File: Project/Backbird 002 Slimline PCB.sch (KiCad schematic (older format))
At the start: 8 parts

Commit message: Upgraded project to KiCad 5 RC2 nightly build (kicad-20180606-033155.9552e02-c4osx)
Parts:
- D1: symbol LED -> Backbird-002-Slimline-PCB-rescue:LED
- Molex_4pin1: symbol Conn_01x04 -> Backbird-002-Slimline-PCB-rescue:Conn_01x04
- R1, R2: symbol R -> Backbird-002-Slimline-PCB-rescue:R
- Sata1, Sata2, SataSlimline1: symbol Conn_01x06 -> Backbird-002-Slimline-PCB-rescue:Conn_01x06
- SataSlimline_Power1: symbol Conn_01x07 -> Backbird-002-Slimline-PCB-rescue:Conn_01x07
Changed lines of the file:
@@
-EESchema Schematic File Version 2
-LIBS:power
-LIBS:device
-LIBS:transistors
-LIBS:conn
-LIBS:linear
-LIBS:regul
-LIBS:74xx
-LIBS:cmos4000
-LIBS:adc-dac
-LIBS:memory
-LIBS:xilinx
-LIBS:microcontrollers
-LIBS:dsp
-LIBS:microchip
-LIBS:analog_switches
-LIBS:motorola
-LIBS:texas
-LIBS:intel
-LIBS:audio
-LIBS:interface
-LIBS:digital-audio
-LIBS:philips
-LIBS:display
-LIBS:cypress
-LIBS:siliconi
-LIBS:opto
-LIBS:atmel
-LIBS:contrib
-LIBS:valves
+EESchema Schematic File Version 4
 LIBS:Backbird 002 Slimline PCB-cache
-EELAYER 25 0
+EELAYER 26 0
 EELAYER END
 $Descr A4 11693 8268
@@
 $EndDescr
 $Comp
-L R R1
+L Backbird-002-Slimline-PCB-rescue:R R1
 U 1 1 5B10C22E
 P 2600 1850
@@
 $EndComp
 $Comp
-L R R2
+L Backbird-002-Slimline-PCB-rescue:R R2
 U 1 1 5B10C260
 P 2600 2350
@@
 $EndComp
 $Comp
-L LED D1
+L Backbird-002-Slimline-PCB-rescue:LED D1
 U 1 1 5B10C28E
 P 2900 2100
@@
 $EndComp
 $Comp
-L Conn_01x04 Molex_4pin1
+L Backbird-002-Slimline-PCB-rescue:Conn_01x04 Molex_4pin1
 U 1 1 5B10C5B0
 P 2950 4450
@@
 +12V\nGND\nGND\n+5V
 $Comp
-L Conn_01x06 Sata1
+L Backbird-002-Slimline-PCB-rescue:Conn_01x06 Sata1
 U 1 1 5B10CD9C
 P 5100 4300
@@
 $EndComp
 $Comp
-L Conn_01x06 SataSlimline1
+L Backbird-002-Slimline-PCB-rescue:Conn_01x06 SataSlimline1
 U 1 1 5B10CE60
 P 5800 1650
@@
 $EndComp
 $Comp
-L Conn_01x07 SataSlimline_Power1
+L Backbird-002-Slimline-PCB-rescue:Conn_01x07 SataSlimline_Power1
 U 1 1 5B10CE99
 P 2950 3500
@@
 Coding\nDevice Presence\n+5V\n+5V\nDiagnostics\nGND\nGND
 $Comp
-L Conn_01x06 Sata2
+L Backbird-002-Slimline-PCB-rescue:Conn_01x06 Sata2
 U 1 1 5B10D3FA
 P 5100 5100
@@
 $EndComp
 Wire Wire Line
-	2600 2000 2600 2200
+	2600 2000 2600 2100
 Wire Wire Line
 	2750 2100 2600 2100
 Connection ~ 2600 2100
 Wire Wire Line
-	2600 2500 2600 4650
+	2600 2500 2600 3500
 Wire Wire Line
 	2600 4650 2750 4650
@@
 Connection ~ 3200 2100
 Wire Wire Line
-	3200 1700 3200 4150
+	3200 1700 3200 2100
 Wire Wire Line
 	3200 4150 2700 4150
 Wire Wire Line
-	2700 3700 2700 4550
+	2700 3700 2700 3800
 Wire Wire Line
 	2700 4550 2750 4550
@@
 Connection ~ 2700 3800
 Wire Wire Line
-	2600 3500 2750 3500
+	2600 3500 2700 3500
 Connection ~ 2600 3500
 Wire Wire Line
@@
 Connection ~ 2700 3500
 Wire Wire Line
-	4900 4100 5500 4100
-Wire Wire Line
-	4850 4200 5450 4200
-Wire Wire Line
-	4800 4300 5400 4300
-Wire Wire Line
-	4750 4400 5350 4400
+	4900 4100 5300 4100
+Wire Wire Line
+	4850 4200 5300 4200
+Wire Wire Line
+	4800 4300 5300 4300
+Wire Wire Line
+	4750 4400 5300 4400
 Wire Wire Line
 	4950 1950 5600 1950
@@
 	5550 5400 5550 4000
 Wire Wire Line
-	5550 4000 4950 4000
+	5550 4000 5300 4000
 Wire Wire Line
 	4950 4000 4950 1950
@@
 Connection ~ 2700 4450
 NoConn ~ 2750 4350
+Wire Wire Line
+	2600 2100 2600 2200
+Wire Wire Line
+	3200 2100 3200 4150
+Wire Wire Line
+	2700 4150 2700 4450
+Wire Wire Line
+	2700 3800 2700 4150
+Wire Wire Line
+	2600 3500 2600 4650
+Wire Wire Line
+	2700 3500 2750 3500
+Wire Wire Line
+	5300 4400 5350 4400
+Wire Wire Line
+	5300 4300 5400 4300
+Wire Wire Line
+	5300 4200 5450 4200
+Wire Wire Line
+	5300 4100 5500 4100
+Wire Wire Line
+	5300 4000 4950 4000
+Wire Wire Line
+	2700 4450 2700 4550
 $EndSCHEMATC

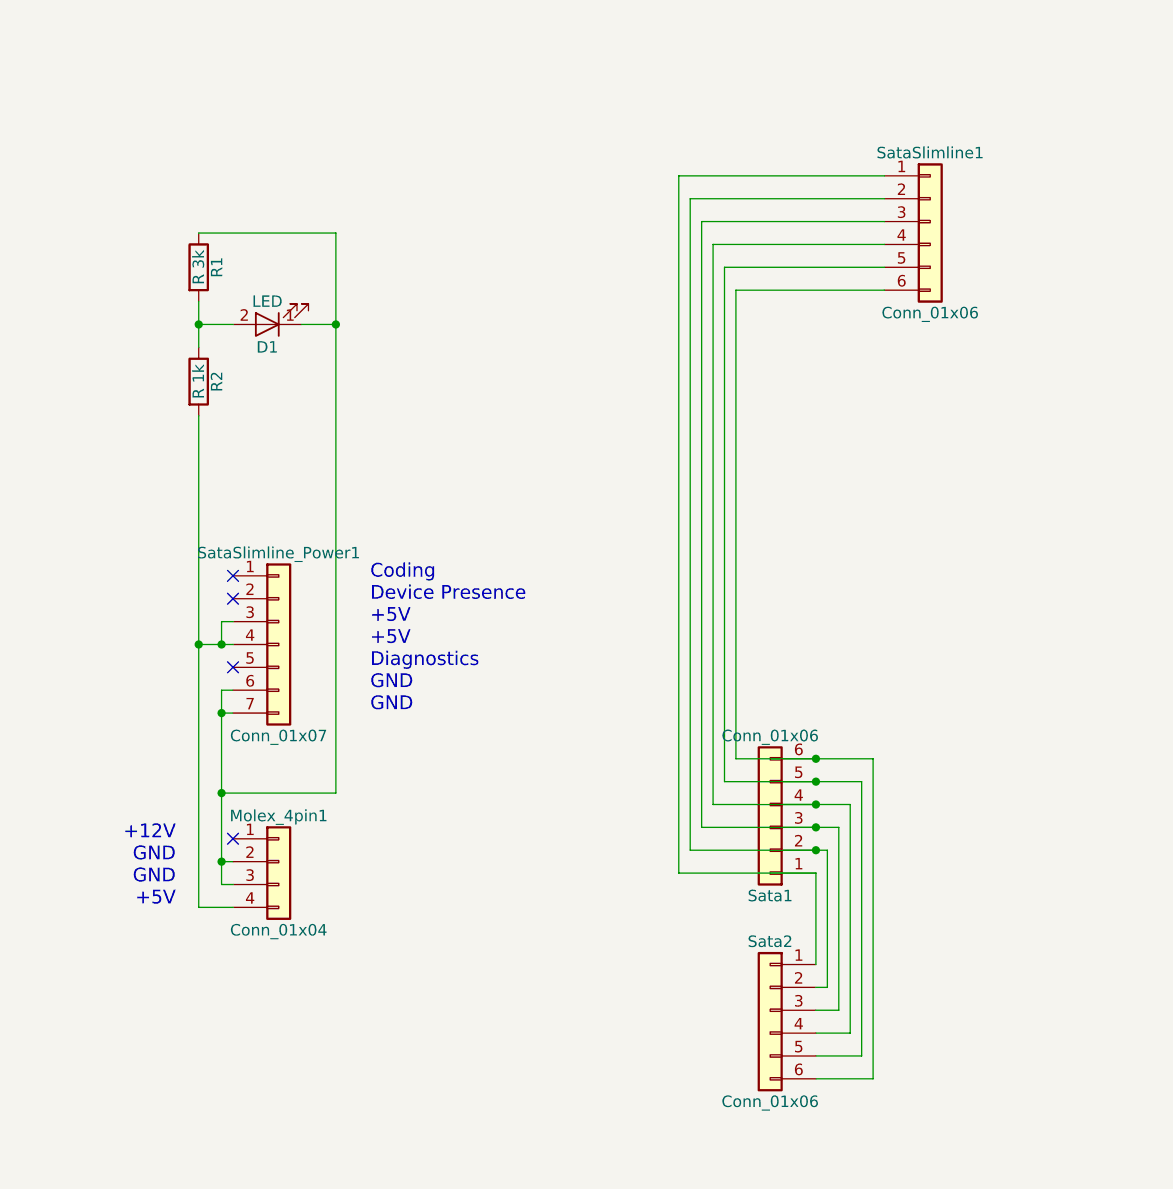
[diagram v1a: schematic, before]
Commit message: Fixed pinout of Sata data ports to be 7-pin instead of 6
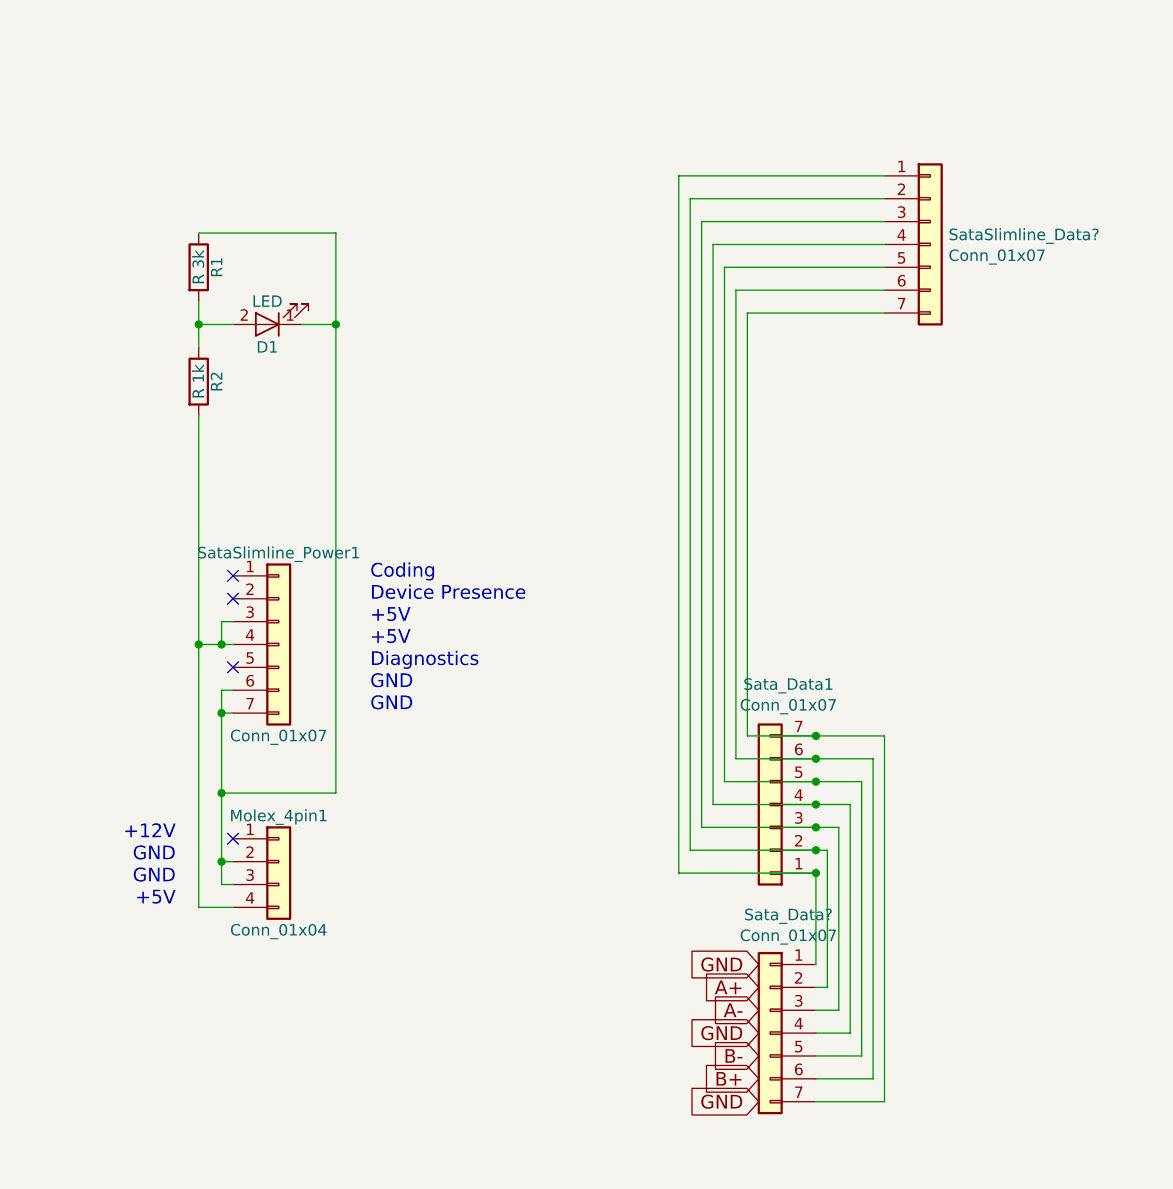
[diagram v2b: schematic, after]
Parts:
- removed Sata1, Sata2, SataSlimline1: Conn_01x06, Connectors:SATA-7_THT_VERT_2, symbol Backbird-002-Slimline-PCB-rescue:Conn_01x06
- added SataSlimline_Data?, Sata_Data1, Sata_Data?: Conn_01x07, symbol Backbird-002-Slimline-PCB-rescue:Conn_01x07
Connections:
- new net: SataSlimline_Data?.1 (Pin_1), Sata_Data1.1 (Pin_1), Sata_Data?.1 (Pin_1)
- new net: SataSlimline_Data?.2 (Pin_2), Sata_Data1.2 (Pin_2), Sata_Data?.2 (Pin_2)
- new net: SataSlimline_Data?.3 (Pin_3), Sata_Data1.3 (Pin_3), Sata_Data?.3 (Pin_3)
- new net: SataSlimline_Data?.4 (Pin_4), Sata_Data1.4 (Pin_4), Sata_Data?.4 (Pin_4)
- new net: SataSlimline_Data?.5 (Pin_5), Sata_Data1.5 (Pin_5), Sata_Data?.5 (Pin_5)
- new net: SataSlimline_Data?.6 (Pin_6), Sata_Data1.6 (Pin_6), Sata_Data?.6 (Pin_6)
- new net: SataSlimline_Data?.7 (Pin_7), Sata_Data1.7 (Pin_7), Sata_Data?.7 (Pin_7)
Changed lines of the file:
@@
 +12V\nGND\nGND\n+5V
-$Comp
-L Backbird-002-Slimline-PCB-rescue:Conn_01x06 Sata1
-U 1 1 5B10CD9C
-P 5100 4300
-F 0 "Sata1" H 5100 4600 50  0000 C CNN
-F 1 "Conn_01x06" H 5100 3900 50  0000 C CNN
-F 2 "Connectors:SATA-7_THT_VERT_2" H 5100 4300 50  0001 C CNN
-F 3 "" H 5100 4300 50  0001 C CNN
-	1    5100 4300
-	-1   0    0    1
-$EndComp
-$Comp
-L Backbird-002-Slimline-PCB-rescue:Conn_01x06 SataSlimline1
-U 1 1 5B10CE60
-P 5800 1650
-F 0 "SataSlimline1" H 5800 1950 50  0000 C CNN
-F 1 "Conn_01x06" H 5800 1250 50  0000 C CNN
-F 2 "Connectors:SATA-7_THT_VERT_2" H 5800 1650 50  0001 C CNN
-F 3 "" H 5800 1650 50  0001 C CNN
-	1    5800 1650
-	1    0    0    -1
-$EndComp
 $Comp
 L Backbird-002-Slimline-PCB-rescue:Conn_01x07 SataSlimline_Power1
@@
 Text Notes 3350 3800 0    60   ~ 0
 Coding\nDevice Presence\n+5V\n+5V\nDiagnostics\nGND\nGND
-$Comp
-L Backbird-002-Slimline-PCB-rescue:Conn_01x06 Sata2
-U 1 1 5B10D3FA
-P 5100 5100
-F 0 "Sata2" H 5100 5400 50  0000 C CNN
-F 1 "Conn_01x06" H 5100 4700 50  0000 C CNN
-F 2 "Connectors:SATA-7_THT_VERT_2" H 5100 5100 50  0001 C CNN
-F 3 "" H 5100 5100 50  0001 C CNN
-	1    5100 5100
-	-1   0    0    -1
-$EndComp
 Wire Wire Line
 	2600 2000 2600 2100
@@
 Wire Wire Line
 	5400 5100 5400 4300
-Connection ~ 5300 4300
 Wire Wire Line
 	5300 5200 5450 5200
 Wire Wire Line
 	5450 5200 5450 4200
-Connection ~ 5300 4200
 Wire Wire Line
 	5300 5300 5500 5300
 Wire Wire Line
 	5500 5300 5500 4100
-Connection ~ 5300 4100
 Wire Wire Line
 	5300 5400 5550 5400
@@
 Wire Wire Line
 	4950 4000 4950 1950
-Connection ~ 5300 4000
 NoConn ~ 2750 3600
 NoConn ~ 2750 3300
@@
 Wire Wire Line
 	2700 4450 2700 4550
+$Comp
+L Backbird-002-Slimline-PCB-rescue:Conn_01x07 Sata_Data1
+U 1 1 5B19C63F
+P 5100 4200
+F 0 "Sata_Data1" H 5020 3675 50  0000 C CNN
+F 1 "Conn_01x07" H 5020 3766 50  0000 C CNN
+F 2 "" H 5100 4200 50  0001 C CNN
+F 3 "" H 5100 4200 50  0001 C CNN
+	1    5100 4200
+	-1   0    0    1
+$EndComp
+Connection ~ 5300 4500
+$Comp
+L Backbird-002-Slimline-PCB-rescue:Conn_01x07 Sata_Data?
+U 1 1 5B19E3C5
+P 5100 5200
+F 0 "Sata_Data?" H 5020 5717 50  0000 C CNN
+F 1 "Conn_01x07" H 5020 5626 50  0000 C CNN
+F 2 "" H 5100 5200 50  0001 C CNN
+F 3 "" H 5100 5200 50  0001 C CNN
+	1    5100 5200
+	-1   0    0    -1
+$EndComp
+Wire Wire Line
+	5300 5500 5600 5500
+Wire Wire Line
+	5600 5500 5600 3900
+Wire Wire Line
+	5600 3900 5300 3900
+$Comp
+L Backbird-002-Slimline-PCB-rescue:Conn_01x07 SataSlimline_Data?
+U 1 1 5B19F411
+P 5800 1750
+F 0 "SataSlimline_Data?" H 5880 1792 50  0000 L CNN
+F 1 "Conn_01x07" H 5880 1701 50  0000 L CNN
+F 2 "" H 5800 1750 50  0001 C CNN
+F 3 "" H 5800 1750 50  0001 C CNN
+	1    5800 1750
+	1    0    0    -1
+$EndComp
+Wire Wire Line
+	5600 2050 5000 2050
+Wire Wire Line
+	5000 2050 5000 3900
+Wire Wire Line
+	5000 3900 5300 3900
+Text GLabel 5050 4900 0    60   Input ~ 0
+GND
+Text GLabel 5050 5200 0    60   Input ~ 0
+GND
+Text GLabel 5050 5000 0    60   Input ~ 0
+A+
+Text GLabel 5050 5100 0    60   Input ~ 0
+A-
+Text GLabel 5050 5300 0    60   Input ~ 0
+B-
+Text GLabel 5050 5400 0    60   Input ~ 0
+B+
+Text GLabel 5050 5500 0    60   Input ~ 0
+GND
+Connection ~ 5300 3900
+Connection ~ 5300 4000
+Connection ~ 5300 4100
+Connection ~ 5300 4200
+Connection ~ 5300 4300
 $EndSCHEMATC

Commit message: Annotated schematic
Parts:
- gave numbers to parts that had none: 2
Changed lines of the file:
@@
 Connection ~ 5300 4500
 $Comp
-L Backbird-002-Slimline-PCB-rescue:Conn_01x07 Sata_Data?
+L Backbird-002-Slimline-PCB-rescue:Conn_01x07 Sata_Data2
 U 1 1 5B19E3C5
 P 5100 5200
-F 0 "Sata_Data?" H 5020 5717 50  0000 C CNN
+F 0 "Sata_Data2" H 5020 5717 50  0000 C CNN
 F 1 "Conn_01x07" H 5020 5626 50  0000 C CNN
 F 2 "" H 5100 5200 50  0001 C CNN
@@
 	5600 3900 5300 3900
 $Comp
-L Backbird-002-Slimline-PCB-rescue:Conn_01x07 SataSlimline_Data?
+L Backbird-002-Slimline-PCB-rescue:Conn_01x07 SataSlimline_Data1
 U 1 1 5B19F411
 P 5800 1750
-F 0 "SataSlimline_Data?" H 5880 1792 50  0000 L CNN
+F 0 "SataSlimline_Data1" H 5880 1792 50  0000 L CNN
 F 1 "Conn_01x07" H 5880 1701 50  0000 L CNN
 F 2 "" H 5800 1750 50  0001 C CNN

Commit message: Added holes for blocking off the LED. Also added an additional connector for power
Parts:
- added Hole1, Hole2: Conn_01x01, symbol Connector:Conn_01x01
- added Power_4pin1: Conn_01x04, Connectors_Molex:Molex_Pico-EZmate_04x1.20mm_Angled, symbol Backbird-002-Slimline-PCB-rescue:Conn_01x04
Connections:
- wire segments 63 -> 69
- no-connect marks 4 -> 3
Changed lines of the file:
@@
 	-1   0    0    1
-$EndComp
-$Comp
-L Backbird-002-Slimline-PCB-rescue:Conn_01x04 Molex_4pin1
-U 1 1 5B10C5B0
-P 2950 4450
-F 0 "Molex_4pin1" H 2950 4650 50  0000 C CNN
-F 1 "Conn_01x04" H 2950 4150 50  0000 C CNN
-F 2 "Connectors_Molex:Molex_Pico-EZmate_04x1.20mm_Angled" H 2950 4450 50  0001 C CNN
-F 3 "" H 2950 4450 50  0001 C CNN
-	1    2950 4450
-	1    0    0    -1
 $EndComp
 Text Notes 2500 4650 2    60   ~ 0
@@
 Connection ~ 2600 2100
 Wire Wire Line
-	2600 2500 2600 3500
-Wire Wire Line
-	2600 4650 2750 4650
+	2600 2500 2600 2800
 Wire Wire Line
 	3050 2100 3200 2100
@@
 	2700 3700 2700 3800
 Wire Wire Line
-	2700 4550 2750 4550
-Wire Wire Line
 	2700 3800 2750 3800
-Connection ~ 2700 4150
 Wire Wire Line
 	2700 3700 2750 3700
@@
 NoConn ~ 2750 3200
 Wire Wire Line
-	2750 4450 2700 4450
-Connection ~ 2700 4450
-NoConn ~ 2750 4350
-Wire Wire Line
 	2600 2100 2600 2200
 Wire Wire Line
-	3200 2100 3200 4150
-Wire Wire Line
-	2700 4150 2700 4450
+	3200 2100 3200 2800
 Wire Wire Line
 	2700 3800 2700 4150
@@
 Connection ~ 5300 4200
 Connection ~ 5300 4300
+$Comp
+L Backbird-002-Slimline-PCB-rescue:Conn_01x04 Power_4pin1
+U 1 1 5B1AF5DD
+P 3650 4450
+F 0 "Power_4pin1" H 3650 4650 50  0000 C CNN
+F 1 "Conn_01x04" H 3650 4150 50  0000 C CNN
+F 2 "Connectors_Molex:Molex_Pico-EZmate_04x1.20mm_Angled" H 3650 4450 50  0001 C CNN
+F 3 "" H 3650 4450 50  0001 C CNN
+	1    3650 4450
+	1    0    0    -1
+$EndComp
+Connection ~ 2700 4450
+Connection ~ 2700 4150
+Wire Wire Line
+	2700 4150 2700 4450
+Wire Wire Line
+	3450 4650 2750 4650
+Wire Wire Line
+	2600 4650 2750 4650
+Connection ~ 2750 4650
+Wire Wire Line
+	2750 4550 3450 4550
+Wire Wire Line
+	2700 4550 2750 4550
+Connection ~ 2750 4550
+Wire Wire Line
+	3450 4450 2750 4450
+Wire Wire Line
+	2750 4450 2700 4450
+Connection ~ 2750 4450
+$Comp
+L Backbird-002-Slimline-PCB-rescue:Conn_01x04 Molex_4pin1
+U 1 1 5B10C5B0
+P 2950 4450
+F 0 "Molex_4pin1" H 2950 4650 50  0000 C CNN
+F 1 "Conn_01x04" H 2950 4150 50  0000 C CNN
+F 2 "Connectors_Molex:Molex_Pico-EZmate_04x1.20mm_Angled" H 2950 4450 50  0001 C CNN
+F 3 "" H 2950 4450 50  0001 C CNN
+	1    2950 4450
+	1    0    0    -1
+$EndComp
+Wire Wire Line
+	2750 4350 3450 4350
+$Comp
+L Connector:Conn_01x01 Hole1
+U 1 1 5B1B7221
+P 2400 2800
+F 0 "Hole1" H 2750 2750 50  0000 R CNN
+F 1 "Conn_01x01" H 3000 2850 50  0000 R CNN
+F 2 "" H 2400 2800 50  0001 C CNN
+F 3 "~" H 2400 2800 50  0001 C CNN
+	1    2400 2800
+	-1   0    0    1
+$EndComp
+Connection ~ 2600 2800
+Wire Wire Line
+	2600 2800 2600 3500
+$Comp
+L Connector:Conn_01x01 Hole2
+U 1 1 5B1B7286
+P 3400 2800
+F 0 "Hole2" H 3480 2842 50  0000 L CNN
+F 1 "Conn_01x01" H 3480 2751 50  0000 L CNN
+F 2 "" H 3400 2800 50  0001 C CNN
+F 3 "~" H 3400 2800 50  0001 C CNN
+	1    3400 2800
+	1    0    0    -1
+$EndComp
+Connection ~ 3200 2800
+Wire Wire Line
+	3200 2800 3200 4150
 $EndSCHEMATC

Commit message: First pass at building the PCB using footprints. Fixed Sata Slimeline Recpt footprint by numbering the pins from 1-13 and adding mechanical pads. Made molex 8981 footprint cleaner by adding the notch.
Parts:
- removed SataSlimline_Data1, SataSlimline_Power1: Conn_01x07, symbol Backbird-002-Slimline-PCB-rescue:Conn_01x07
- added Sata_Slimline_Recpt1: Conn_01x13, ProjectFootprints:SATA_SLIMLINE_RECPT_1735539-2, symbol Connector:Conn_01x13
- added Screw_Hole_B, Screw_Hole_T?: Conn_01x01, symbol Connector:Conn_01x01
- +5V_Hole1: renamed from Hole1; footprint (none) -> Wire_Pads:SolderWirePad_single_1-2mmDrill
- D1: footprint (none) -> LEDs:LED_D1.8mm_W3.3mm_H2.4mm
- GND_Hole2: renamed from Hole2; footprint (none) -> Wire_Pads:SolderWirePad_single_1-2mmDrill
- Molex_4pin1: footprint Connectors_Molex:Molex_Pico-EZmate_04x1.20mm_Angled -> ProjectFootprints:MOLEX_8981_0015244745
- Power_4pin1: footprint Connectors_Molex:Molex_Pico-EZmate_04x1.20mm_Angled -> Wire_Pads:SolderWirePad_4xInline_1-2mmDrill
- R1, R2: footprint (none) -> Resistors_Universal:Resistor_SMD+THTuniversal_2512_RM10_HandSoldering
- Sata_Data1, Sata_Data2: footprint (none) -> ProjectFootprints:SATA_DATA_678007005_CustomPad
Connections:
- net labels added: +12V, +5V
- wire segments 69 -> 8
- no-connect marks 3 -> 4
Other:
- note removed: "+12V\nGND\nGND\n+5V"
- note removed: "Coding\nDevice Presence\n+5V\n+5V\nDiagnostics\nGND\nGND"
- moved on the sheet: D1, Molex_4pin1, Power_4pin1, R1, R2, Sata_Data1, Sata_Data2

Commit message: Updated PSB layout. (might remove extra power and Sata locations) Added custom footprints for screws and for a generic 8981 power pinout.
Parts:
- Power_4pin1: footprint Wire_Pads:SolderWirePad_4xInline_1-2mmDrill -> ProjectFootprints:MOLEX_8981_Generic
- Screw_Hole_B1: renamed from Screw_Hole_B; footprint (none) -> ProjectFootprints:Blackbird002_Slimline_PCB_Screw
- Screw_Hole_T1: renamed from Screw_Hole_T?; footprint (none) -> ProjectFootprints:Blackbird002_Slimline_PCB_Screw
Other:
- moved on the sheet: Power_4pin1
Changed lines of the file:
@@
 L Backbird-002-Slimline-PCB-rescue:Conn_01x04 Power_4pin1
 U 1 1 5B1AF5DD
-P 3900 5450
-F 0 "Power_4pin1" H 3900 5650 50  0000 C CNN
-F 1 "Conn_01x04" H 3900 5150 50  0000 C CNN
-F 2 "Wire_Pads:SolderWirePad_4xInline_1-2mmDrill" H 3900 5450 50  0001 C CNN
-F 3 "" H 3900 5450 50  0001 C CNN
-	1    3900 5450
+P 4550 5450
+F 0 "Power_4pin1" H 4550 5650 50  0000 C CNN
+F 1 "Conn_01x04" H 4550 5150 50  0000 C CNN
+F 2 "ProjectFootprints:MOLEX_8981_Generic" H 4550 5450 50  0001 C CNN
+F 3 "" H 4550 5450 50  0001 C CNN
+	1    4550 5450
 	1    0    0    -1
 $EndComp
@@
 Text GLabel 3550 3050 0    60   Input ~ 0
 GND
-Text GLabel 3700 5650 0    60   Input ~ 0
+Text GLabel 4350 5650 0    60   Input ~ 0
 +5V
-Text GLabel 3700 5550 0    60   Input ~ 0
+Text GLabel 4350 5550 0    60   Input ~ 0
 GND
-Text GLabel 3700 5450 0    60   Input ~ 0
+Text GLabel 4350 5450 0    60   Input ~ 0
 GND
-Text GLabel 3700 5350 0    60   Input ~ 0
+Text GLabel 4350 5350 0    60   Input ~ 0
 +12V
 $Comp
-L Connector:Conn_01x01 Screw_Hole_B
+L Connector:Conn_01x01 Screw_Hole_B1
 U 1 1 5B1E13D1
 P 2850 3900
-F 0 "Screw_Hole_B" H 2929 3942 50  0000 L CNN
+F 0 "Screw_Hole_B1" H 2929 3942 50  0000 L CNN
 F 1 "Conn_01x01" H 2929 3851 50  0000 L CNN
-F 2 "" H 2850 3900 50  0001 C CNN
+F 2 "ProjectFootprints:Blackbird002_Slimline_PCB_Screw" H 2850 3900 50  0001 C CNN
 F 3 "~" H 2850 3900 50  0001 C CNN
 	1    2850 3900
@@
 NoConn ~ 2650 3900
 $Comp
-L Connector:Conn_01x01 Screw_Hole_T?
+L Connector:Conn_01x01 Screw_Hole_T1
 U 1 1 5B1E164C
 P 2500 1350
-F 0 "Screw_Hole_T?" H 2579 1392 50  0000 L CNN
+F 0 "Screw_Hole_T1" H 2579 1392 50  0000 L CNN
 F 1 "Conn_01x01" H 2579 1301 50  0000 L CNN
-F 2 "" H 2500 1350 50  0001 C CNN
+F 2 "ProjectFootprints:Blackbird002_Slimline_PCB_Screw" H 2500 1350 50  0001 C CNN
 F 3 "~" H 2500 1350 50  0001 C CNN
 	1    2500 1350
